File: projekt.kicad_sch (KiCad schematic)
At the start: 116 parts, among them IC1 DW01+G, IC4 MIC5504-3.3YM5-TR, J1 10118194-0001LF, J10 Conn_01x06_Pin, J2 TP4056, J4 Conn_01x02_Socket, Q1 AO3400A, Q2 AO3400A, Q3 AO3400A, Q4 AO3400A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

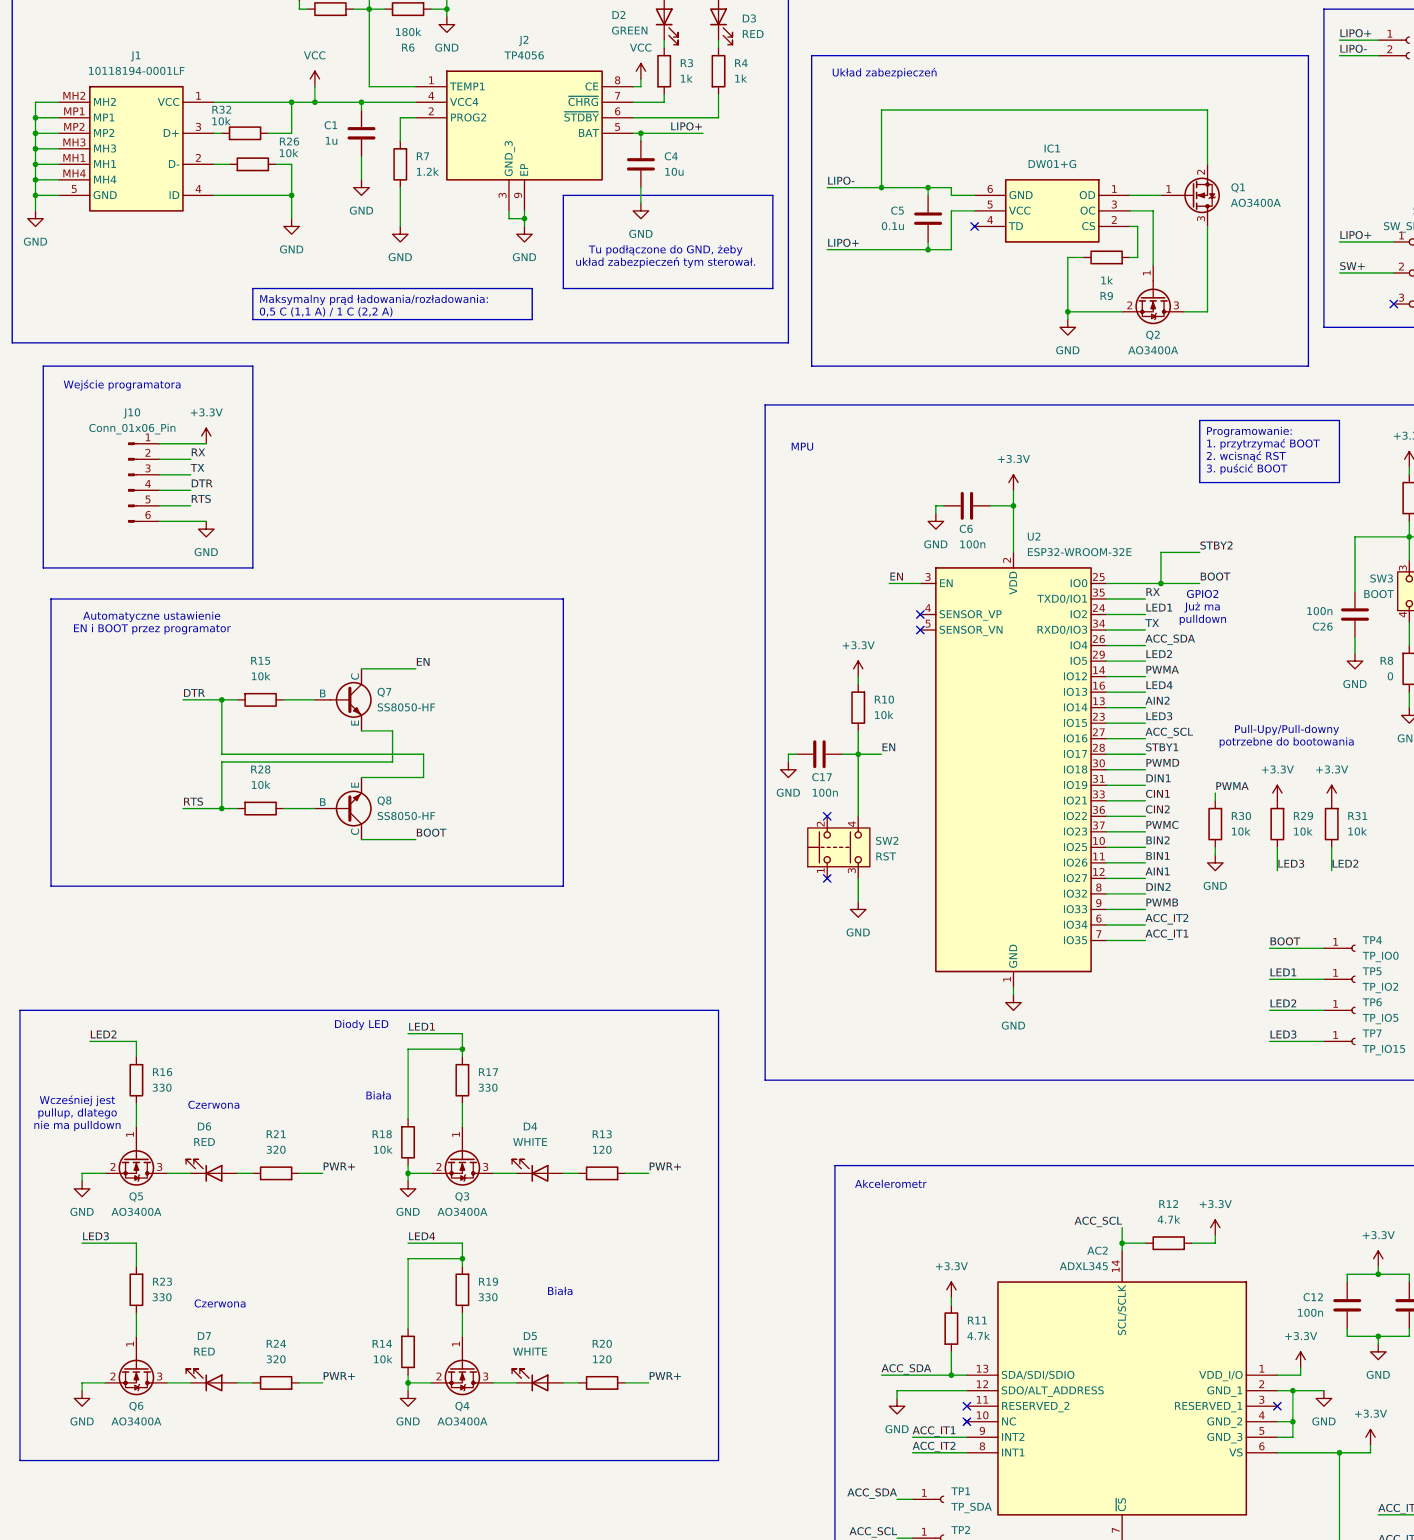
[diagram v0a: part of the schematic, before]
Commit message: Podmiana tranzystorów
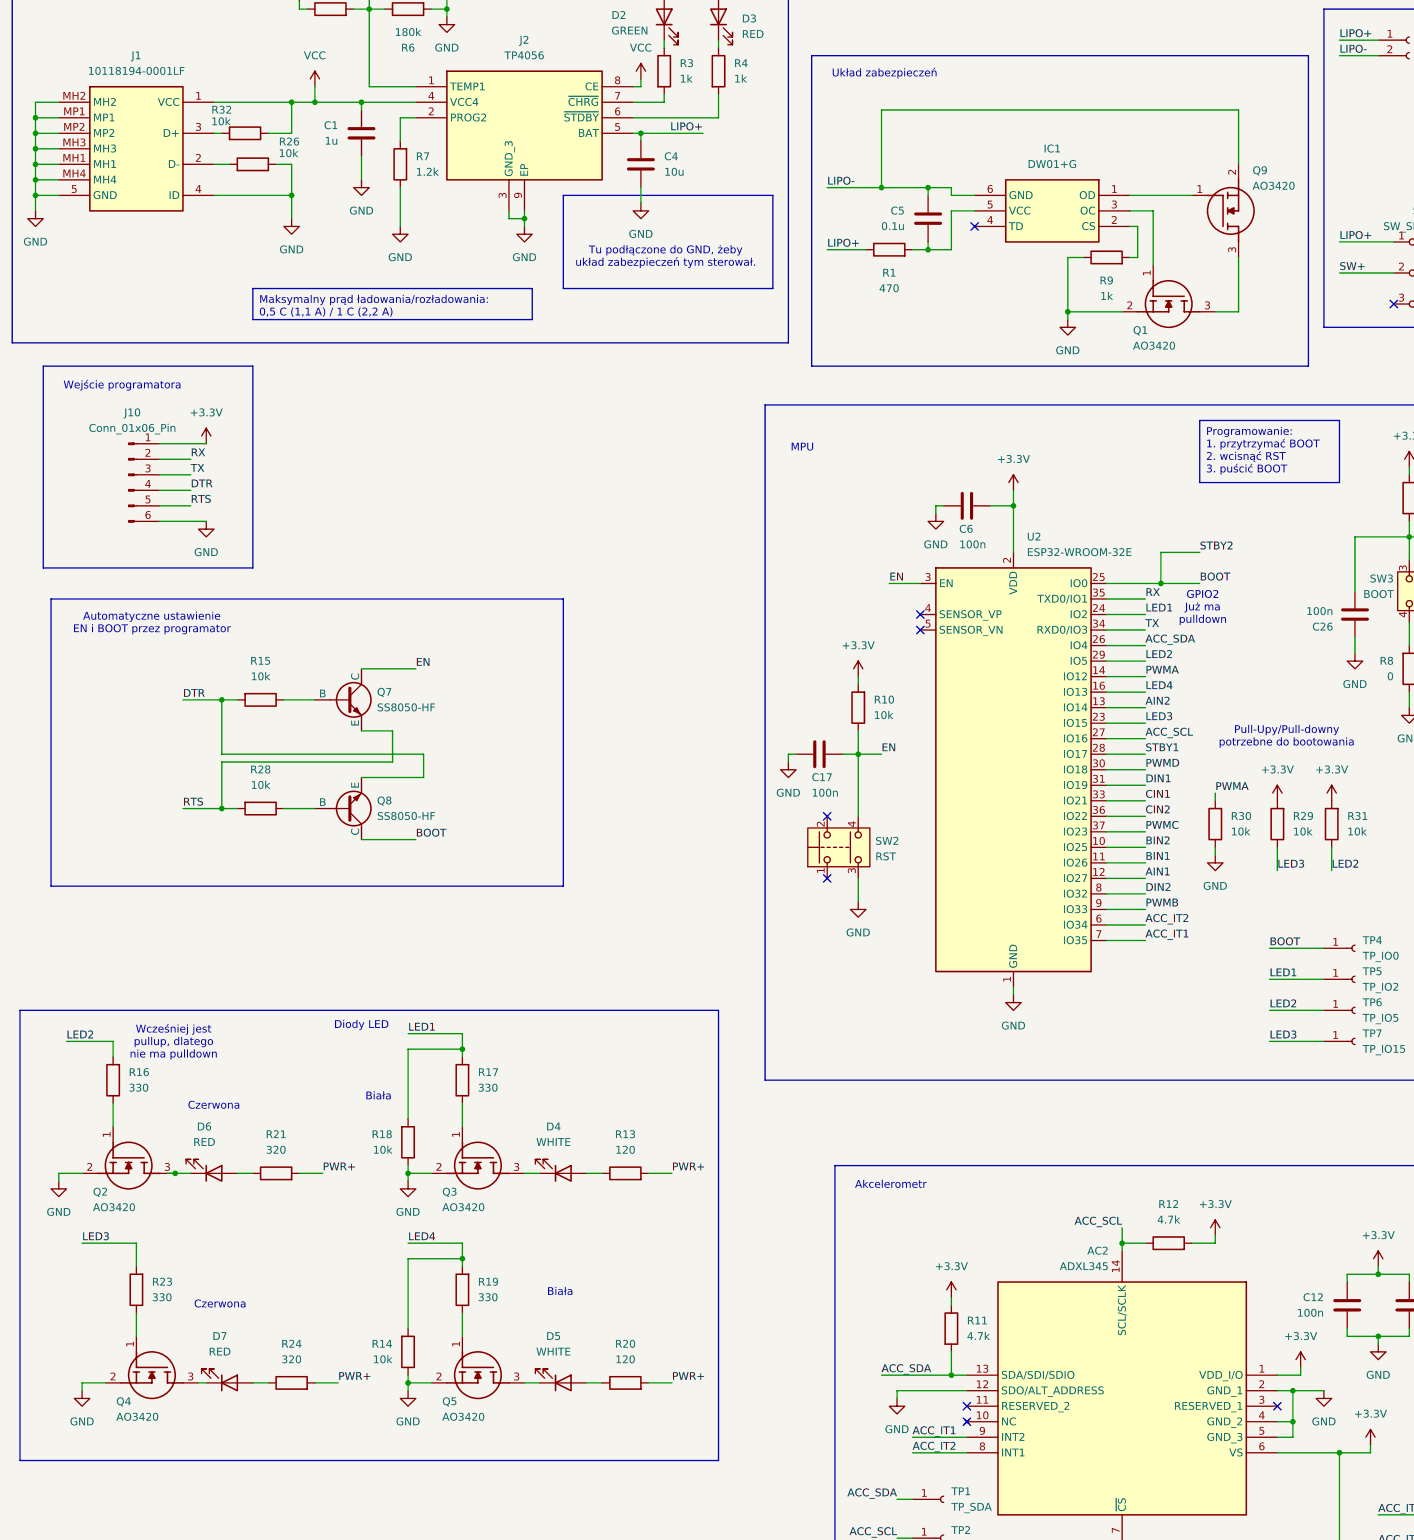
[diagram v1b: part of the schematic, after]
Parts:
- removed Q1, Q2, Q3, Q4, Q5, Q6: AO3400A, Package_TO_SOT_SMD:SOT-23, symbol Transistor_FET:AO3400A
- added Q1, Q2, Q3, Q4, Q5, Q9: AO3420, SOT95P280X125-3N, symbol SamacSys_Parts:AO3420
- added R1: 470, Resistor_SMD:R_0603_1608Metric_Pad0.98x0.95mm_HandSolder, symbol Device:R
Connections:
- net GND: now also Q1.2 (S), Q2.2 (S), Q3.2 (S), Q4.2 (S), Q5.2 (S)
- net LIPO+: now also R1.1; no longer C5.2, IC1.5 (VCC)
- net LIPO-: now also Q9.2 (S)
- net at R19.1: now also Q5.1 (G)
- net at D4.1 (K): now also Q3.3 (D)
- net at D5.1 (K): now also Q5.3 (D)
- net at R17.1: now also Q3.1 (G)
- net at R23.1: now also Q4.1 (G)
- net at D6.1 (K): now also Q2.3 (D)
- net at R16.1: now also Q2.1 (G)
- net at IC1.1 (OD): now also Q9.1 (G)
- net at D7.1 (K): now also Q4.3 (D)
- net at IC1.3 (OC): now also Q1.1 (G)
- new net: Q1.3 (D), Q9.3 (D)
- new net: C5.2, IC1.5 (VCC), R1.2
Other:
- moved on the sheet: D4, D5, D7, R13, R16, R20, R24

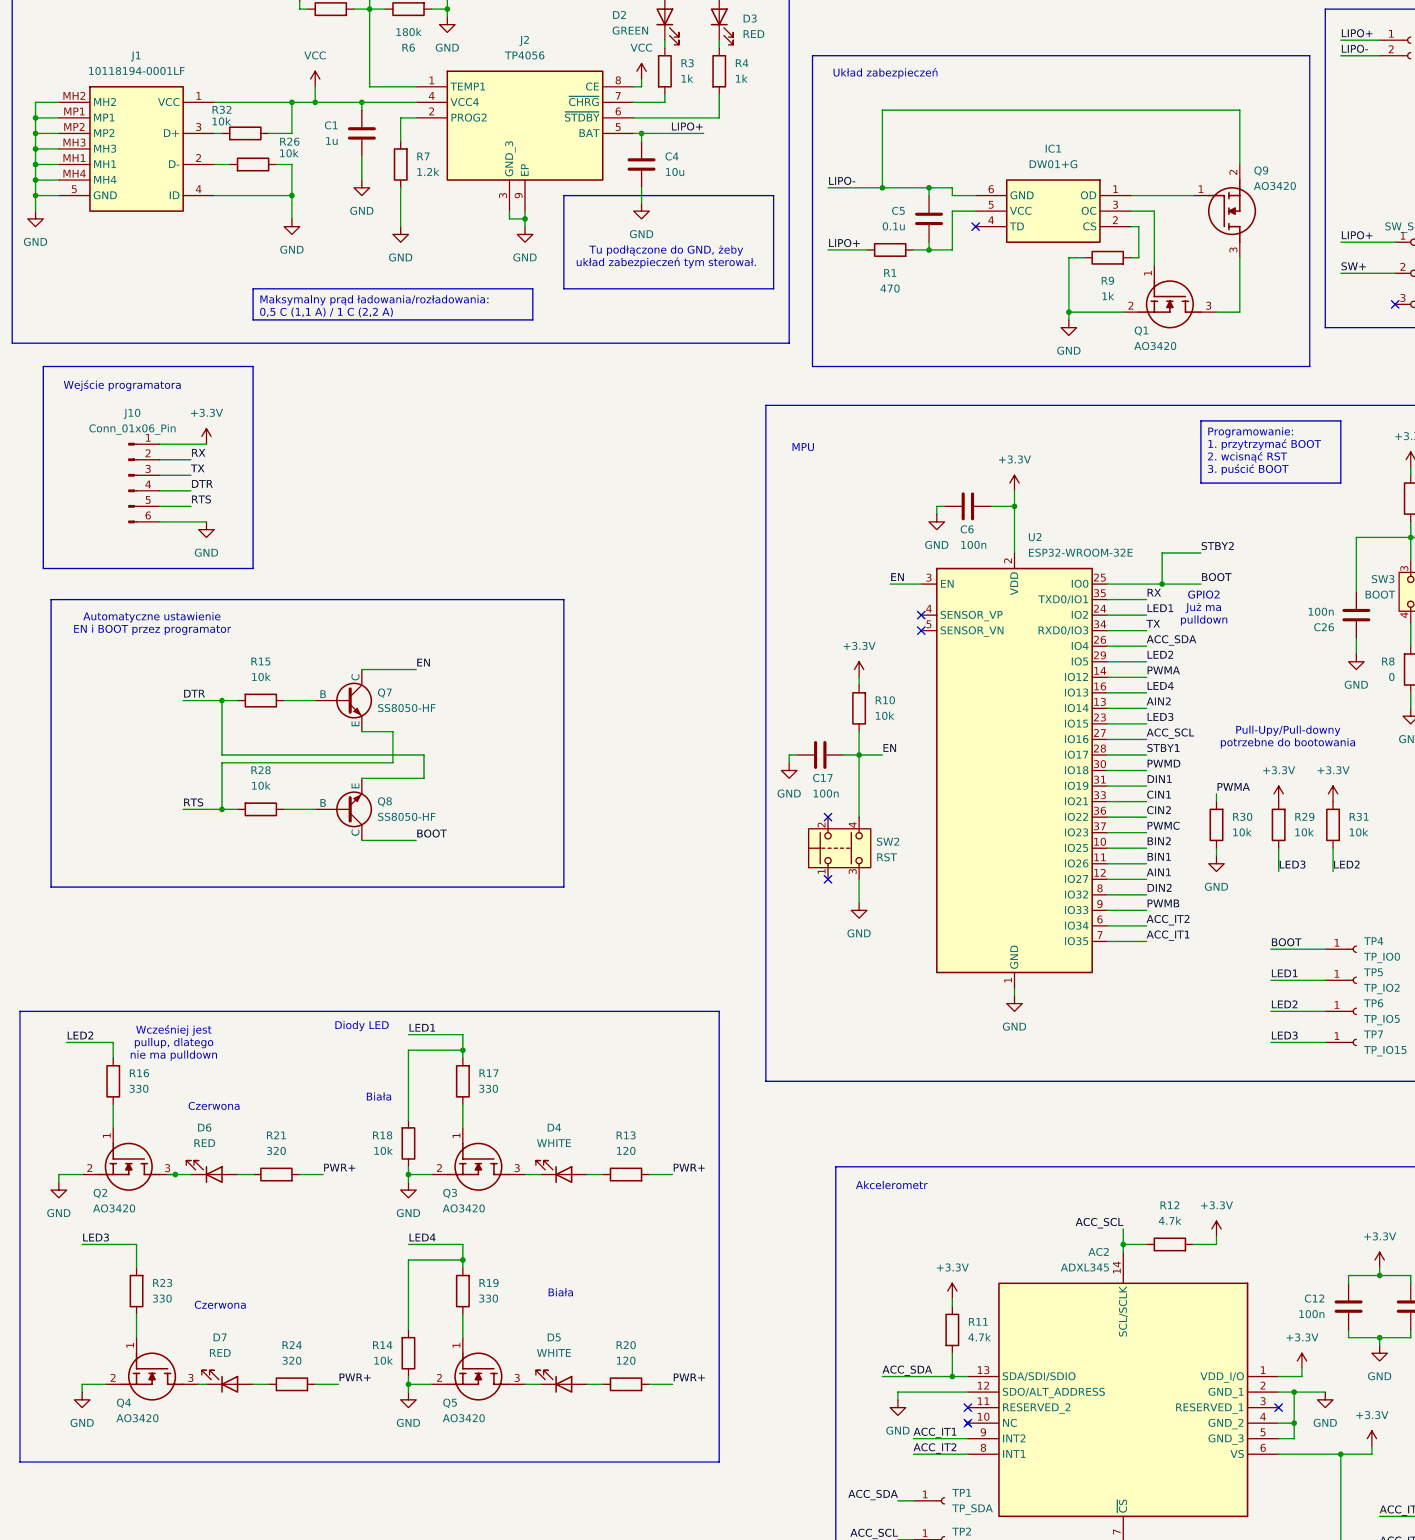
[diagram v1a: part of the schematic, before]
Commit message: Podmiana tranzystorów i symboli
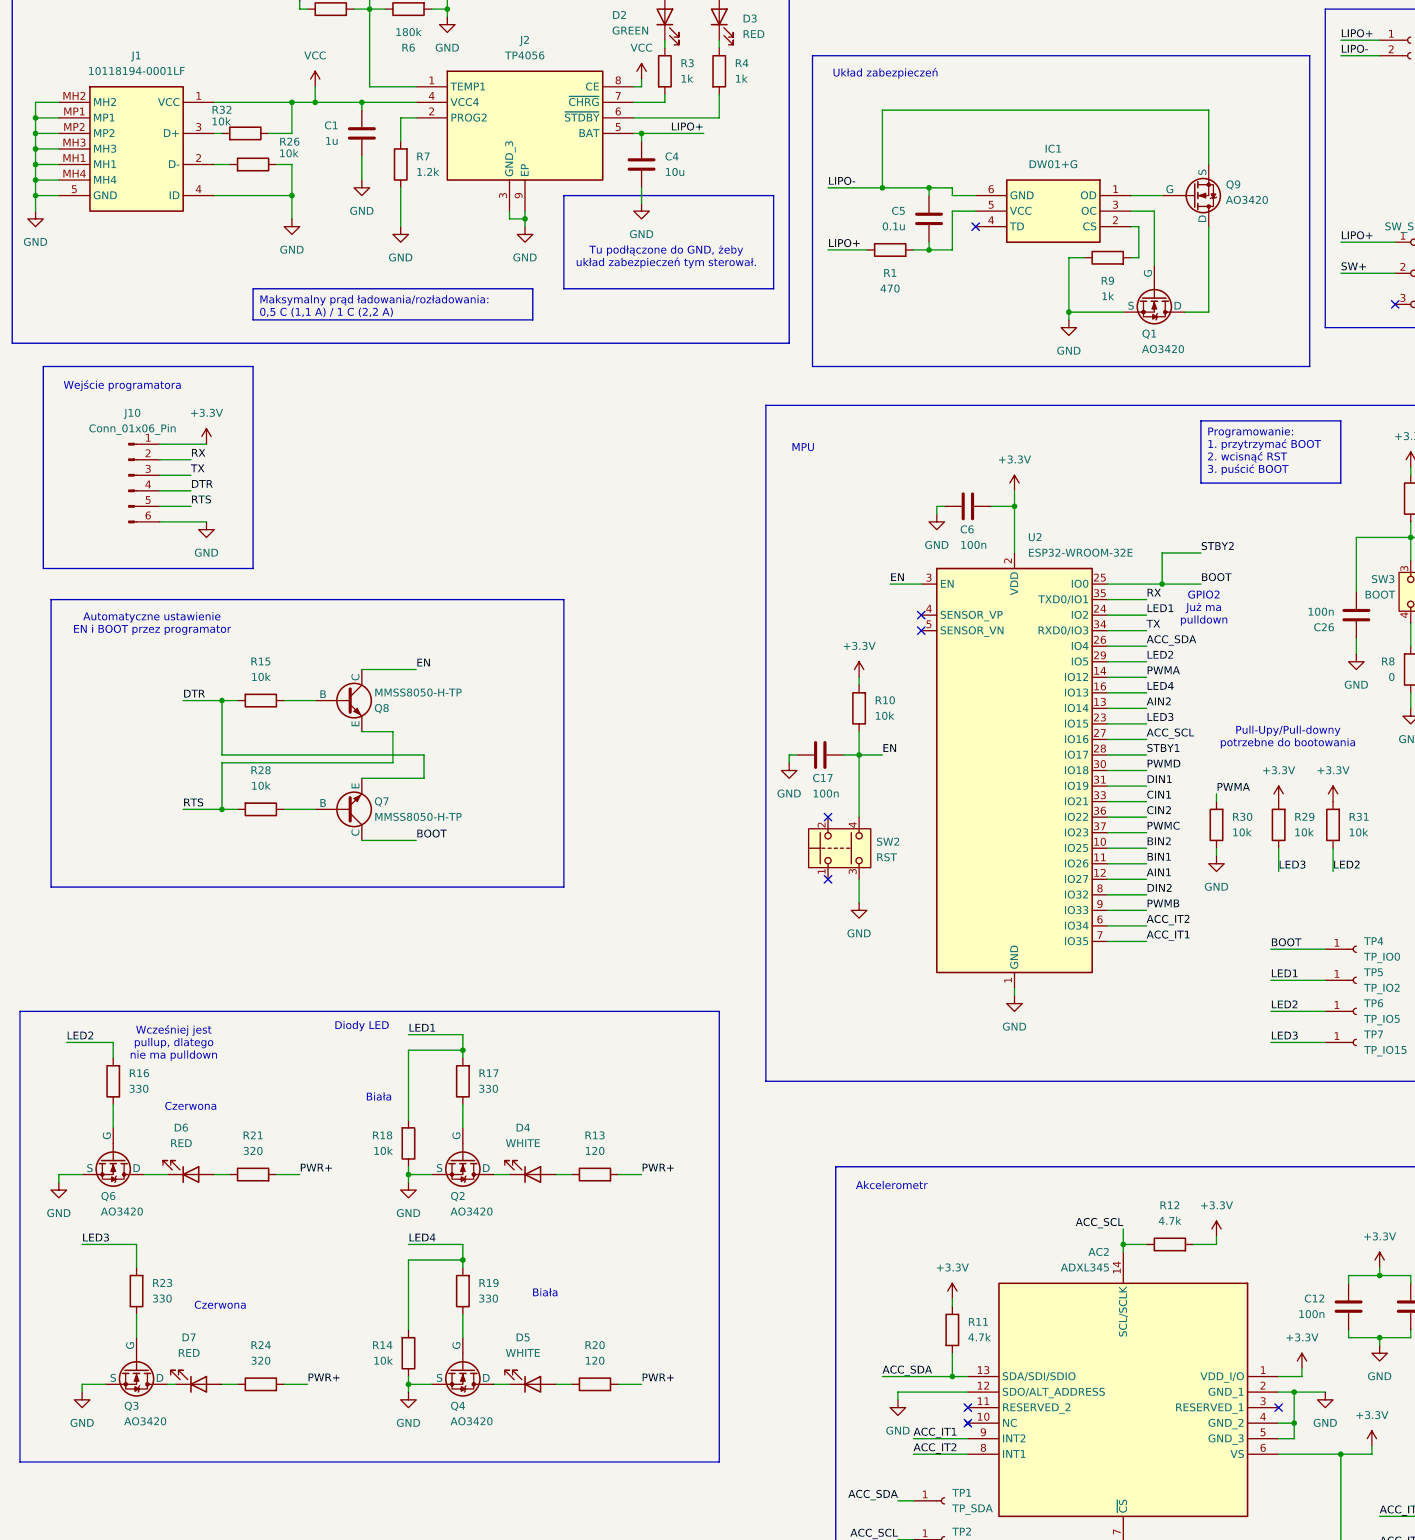
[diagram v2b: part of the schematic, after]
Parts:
- removed Q2, Q3, Q4, Q5: AO3420, SOT95P280X125-3N, symbol SamacSys_Parts:AO3420
- added Q2, Q3, Q4, Q6: AO3420, SOT95P280X125-3N, symbol Simulation_SPICE:NMOS
- Q1, Q9: symbol SamacSys_Parts:AO3420 -> Simulation_SPICE:NMOS
- Q7, Q8: value SS8050-HF -> MMSS8050-H-TP; footprint SOT95P240X115-3N -> SOT95P237X125-3N; Height (none) -> 1.25; Manufacturer_Name (none) -> MCC; Manufacturer_Part_Number (none) -> MMSS8050-H-TP
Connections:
- net BOOT: now also Q7.3 (C); no longer Q8.1 (C)
- net DTR: now also Q7.2 (E); no longer Q8.3 (E)
- net EN: now also Q8.3 (C); no longer Q7.1 (C)
- net GND: now also Q2.2 (S), Q3.2 (S), Q4.2 (S), Q6.2 (S)
- net RTS: now also Q8.2 (E); no longer Q7.3 (E)
- net at R19.1: now also Q4.1 (G)
- net at D4.1 (K): now also Q2.3 (D)
- net at R28.1: now also Q7.1 (B); no longer Q8.2 (B)
- net at D5.1 (K): now also Q4.3 (D)
- net at R16.1: now also Q6.1 (G)
- net at D6.1 (K): now also Q6.3 (D)
- net at R23.1: now also Q3.1 (G)
- net at D7.1 (K): now also Q3.3 (D)
- net at R17.1: now also Q2.1 (G)
- net at R15.1: now also Q8.1 (B); no longer Q7.2 (B)
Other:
- moved on the sheet: D4, D5, D6, D7, R13, R20, R21, R24
